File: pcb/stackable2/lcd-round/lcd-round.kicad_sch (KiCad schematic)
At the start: 10 parts, among them J1 JST SH, J2 Pin headers, J3 Pin headers, Q1 BSS138

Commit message: Migrate `SOT-23` footprint to `packages`
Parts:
- Q1: footprint custom:SOT-23_simple -> packages:SOT-23
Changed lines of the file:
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@@
 			)
 		)
-		(property "Footprint" "custom:SOT-23_simple"
+		(property "Footprint" "packages:SOT-23"
 			(at 143.51 136.525 0)
 			(effects

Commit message: Rename `connectors` symbol and footprint libraries to `connector`
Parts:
- J1: footprint connectors:JST_SH_SM08B-SRSS-TB_1x08-1MP_P1.00mm_Horizontal -> connector:JST_SH_SM08B-SRSS-TB_1x08-1MP_P1.00mm_Horizontal
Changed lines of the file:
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@@
 			)
 		)
-		(property "Footprint" "connectors:JST_SH_SM08B-SRSS-TB_1x08-1MP_P1.00mm_Horizontal"
+		(property "Footprint" "connector:JST_SH_SM08B-SRSS-TB_1x08-1MP_P1.00mm_Horizontal"
 			(at 193.04 105.41 0)
 			(effects

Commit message: Rename `modules` symbol and footprint libraries to `module`
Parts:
- LCD1: footprint modules:GC9A01-screen-connector-pads -> module:GC9A01-screen-connector-pads; symbol modules:LCD-round-1.28in-GC9A01 -> module:LCD-round-1.28in-GC9A01
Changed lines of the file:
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@@
 	)
 	(symbol
-		(lib_id "modules:LCD-round-1.28in-GC9A01")
+		(lib_id "module:LCD-round-1.28in-GC9A01")
 		(at 132.08 87.63 0)
 		(unit 1)
@@
 			)
 		)
-		(property "Footprint" "modules:GC9A01-screen-connector-pads"
+		(property "Footprint" "module:GC9A01-screen-connector-pads"
 			(at 132.588 93.726 0)
 			(effects

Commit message: Rename `packages` footprint library to `package`
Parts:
- Q1: footprint packages:SOT-23 -> package:SOT-23
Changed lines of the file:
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@@
 			)
 		)
-		(property "Footprint" "packages:SOT-23"
+		(property "Footprint" "package:SOT-23"
 			(at 143.51 136.525 0)
 			(effects

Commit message: Migrate 0603 capacitor hand soldering footprint to `discrete`
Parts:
- C1, C2: footprint custom:C_0603_1608Metric_Pad1.08x0.95mm_HandSolder -> discrete:C_0603_1608Metric_Pad1.08x0.95mm_HandSolder
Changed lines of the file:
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@@
 			)
 		)
-		(property "Footprint" "custom:C_0603_1608Metric_Pad1.08x0.95mm_HandSolder"
+		(property "Footprint" "discrete:C_0603_1608Metric_Pad1.08x0.95mm_HandSolder"
 			(at 100.33 87.63 0)
 			(effects
@@
 			)
 		)
-		(property "Footprint" "custom:C_0603_1608Metric_Pad1.08x0.95mm_HandSolder"
+		(property "Footprint" "discrete:C_0603_1608Metric_Pad1.08x0.95mm_HandSolder"
 			(at 90.17 87.63 0)
 			(effects

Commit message: Update lcd-round to use KiCAD built-in discrete footprints
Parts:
- Q1: footprint package:SOT-23 -> Package_TO_SOT_SMD:SOT-23
- R1, R2, R3: footprint custom:R_0603_1608Metric_Pad0.98x0.95mm_HandSolder_simple -> Resistor_SMD:R_0603_1608Metric_Pad0.98x0.95mm_HandSolder
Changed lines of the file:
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@@
 			)
 		)
-		(property "Footprint" "custom:R_0603_1608Metric_Pad0.98x0.95mm_HandSolder_simple"
+		(property "Footprint" "Resistor_SMD:R_0603_1608Metric_Pad0.98x0.95mm_HandSolder"
 			(at 130.81 138.43 0)
 			(effects
@@
 			)
 		)
-		(property "Footprint" "custom:R_0603_1608Metric_Pad0.98x0.95mm_HandSolder_simple"
+		(property "Footprint" "Resistor_SMD:R_0603_1608Metric_Pad0.98x0.95mm_HandSolder"
 			(at 171.45 80.01 0)
 			(effects
@@
 			)
 		)
-		(property "Footprint" "package:SOT-23"
+		(property "Footprint" "Package_TO_SOT_SMD:SOT-23"
 			(at 143.51 136.525 0)
 			(effects
@@
 			)
 		)
-		(property "Footprint" "custom:R_0603_1608Metric_Pad0.98x0.95mm_HandSolder_simple"
+		(property "Footprint" "Resistor_SMD:R_0603_1608Metric_Pad0.98x0.95mm_HandSolder"
 			(at 130.81 129.54 0)
 			(effects

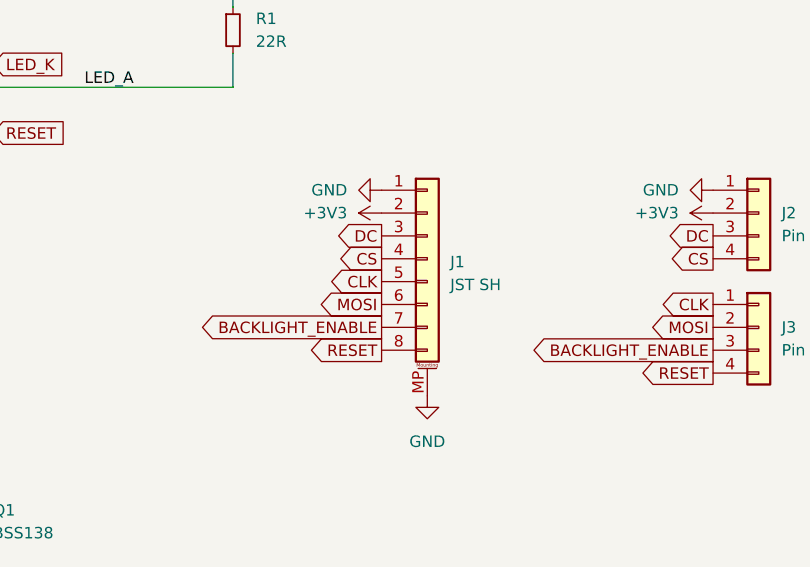
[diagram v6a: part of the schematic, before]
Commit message: Use new JST SH GC9A01 LCD connector symbol in stackable2/lcd-round
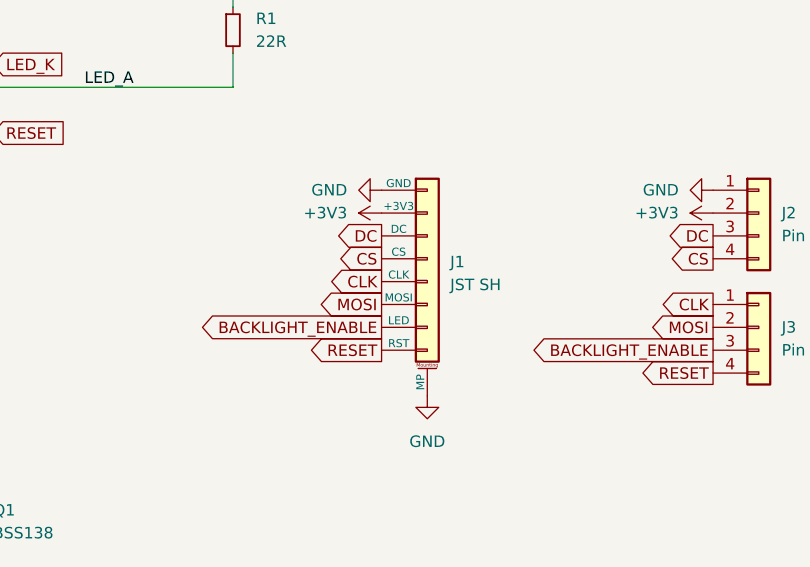
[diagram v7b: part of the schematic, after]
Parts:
- removed J1: JST SH, connector:JST_SH_SM08B-SRSS-TB_1x08-1MP_P1.00mm_Horizontal, symbol Connector_Generic_MountingPin:Conn_01x08_MountingPin
- added J1: JST SH, connector:JST_SH_SM08B-SRSS-TB_1x08-1MP_P1.00mm_Horizontal, symbol connector:JST_SH_01x08_GC9A01
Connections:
- net +3V3: now also J1.2 (+3V3)
- net BACKLIGHT_ENABLE: now also J1.7 (LED)
- net CLK: now also J1.5 (CLK)
- net CS: now also J1.4 (CS)
- net DC: now also J1.3 (DC)
- net GND: now also J1.1 (GND), J1.MP
- net MOSI: now also J1.6 (MOSI)
- net RESET: now also J1.8 (RST)
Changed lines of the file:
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@@
 	(label "LED_A"
 		(at 154.94 86.36 0)
-		(fields_autoplaced yes)
 		(effects
 			(font
@@
 	)
 	(symbol
+		(lib_id "connector:JST_SH_01x08_GC9A01")
+		(at 193.04 105.41 0)
+		(unit 1)
+		(exclude_from_sim no)
+		(in_bom yes)
+		(on_board yes)
+		(dnp no)
+		(fields_autoplaced yes)
+		(property "Reference" "J1"
+			(at 195.58 105.7655 0)
+			(effects
+				(font
+					(size 1.27 1.27)
+				)
+				(justify left)
+			)
+		)
+		(property "Value" "JST SH"
+			(at 195.58 108.3055 0)
+			(effects
+				(font
+					(size 1.27 1.27)
+				)
+				(justify left)
+			)
+		)
+		(property "Footprint" "connector:JST_SH_SM08B-SRSS-TB_1x08-1MP_P1.00mm_Horizontal"
+			(at 193.04 105.41 0)
+			(effects
+				(font
+					(size 1.27 1.27)
+				)
+				(hide yes)
+			)
+		)
+		(property "Datasheet" "~"
+			(at 193.04 105.41 0)
+			(effects
+				(font
+					(size 1.27 1.27)
+				)
+				(hide yes)
+			)
+		)
+		(property "Description" "JST SH connector for GC9A01 round LCD"
+			(at 193.04 105.41 0)
+			(effects
+				(font
+					(size 1.27 1.27)
+				)
+				(hide yes)
+			)
+		)
+		(property "LCSC Part" "C7433429"
+			(at 193.04 105.41 0)
+			(effects
+				(font
+					(size 1.27 1.27)
+				)
+				(hide yes)
+			)
+		)
+		(pin "MP"
+		)
+		(pin "7"
+		)
+		(pin "6"
+		)
+		(pin "4"
+		)
+		(pin "5"
+		)
+		(pin "8"
+		)
+		(pin "2"
+		)
+		(pin "3"
+		)
+		(pin "1"
+		)
+		(instances
+			(project ""
+				(path "/76a56607-25e2-40a3-9282-ff279b153f75"
+					(reference "J1")
+					(unit 1)
+				)
+			)
+		)
+	)
+	(symbol
 		(lib_id "Device:R_Small")
 		(at 130.81 138.43 0)
@@
 					(unit 1)
 				)
-			)
-		)
-	)
-	(symbol
-		(lib_id "Connector_Generic_MountingPin:Conn_01x08_MountingPin")
-		(at 193.04 105.41 0)
-		(unit 1)
-		(exclude_from_sim no)
-		(in_bom yes)
-		(on_board yes)
-		(dnp no)
-		(fields_autoplaced yes)
-		(property "Reference" "J1"
-			(at 195.58 105.7655 0)
-			(effects
-				(font
-					(size 1.27 1.27)
-				)
-				(justify left)
-			)
-		)
-		(property "Value" "JST SH"
-			(at 195.58 108.3055 0)
-			(effects
-				(font
-					(size 1.27 1.27)
-				)
-				(justify left)
-			)
-		)
-		(property "Footprint" "connector:JST_SH_SM08B-SRSS-TB_1x08-1MP_P1.00mm_Horizontal"
-			(at 193.04 105.41 0)
-			(effects
-				(font
-					(size 1.27 1.27)
-				)
-				(hide yes)
-			)
-		)
-		(property "Datasheet" "~"
-			(at 193.04 105.41 0)
-			(effects
-				(font
-					(size 1.27 1.27)
-				)
-				(hide yes)
-			)
-		)
-		(property "Description" "Generic connectable mounting pin connector, single row, 01x08, script generated (kicad-library-utils/schlib/autogen/connector/)"
-			(at 193.04 105.41 0)
-			(effects
-				(font
-					(size 1.27 1.27)
-				)
-				(hide yes)
-			)
-		)
-		(pin "1"
-		)
-		(pin "2"
-		)
-		(pin "3"
-		)
-		(pin "MP"
-		)
-		(pin "7"
-		)
-		(pin "6"
-		)
-		(pin "5"
-		)
-		(pin "8"
-		)
-		(pin "4"
-		)
-		(instances
-			(project ""
-				(path "/76a56607-25e2-40a3-9282-ff279b153f75"
-					(reference "J1")
-					(unit 1)
-				)
